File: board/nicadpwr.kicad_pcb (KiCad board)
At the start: 2 copper layers, 60.2 x 20.6 mm, 31 parts, among them P1 CONN_SENSE, P2 CONN_CHARGE, P3 CONN_BAT, P4 CONN_VOUT, Q1 2N7000, Q2 BC547, Q3 TPCA8052H, U1 LM317T, U2 LM1117-5.0, U3 MC34063A

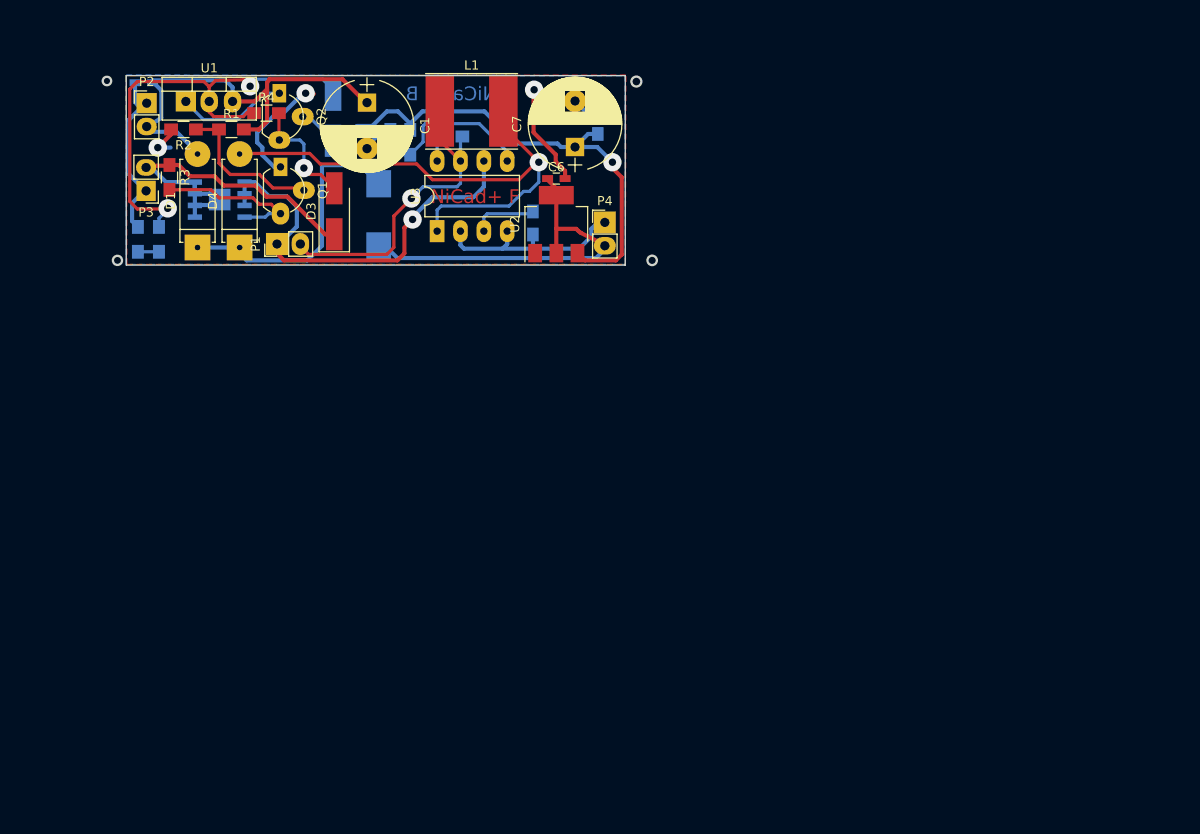
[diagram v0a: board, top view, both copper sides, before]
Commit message: Redesign of the board with fixes...
1. The charging voltage is now 5V (suitable for charging from USB)
   The charging now is connected directly to boost converter and
   linear out and battery charger are connected to the boost output.
   The converter raises battery or charging voltage to 6.3 volt.
2. Fixed problem with n-channel FET switch by using p-channel high
   side FET.
3. The board is enlarged and made single copper layer.
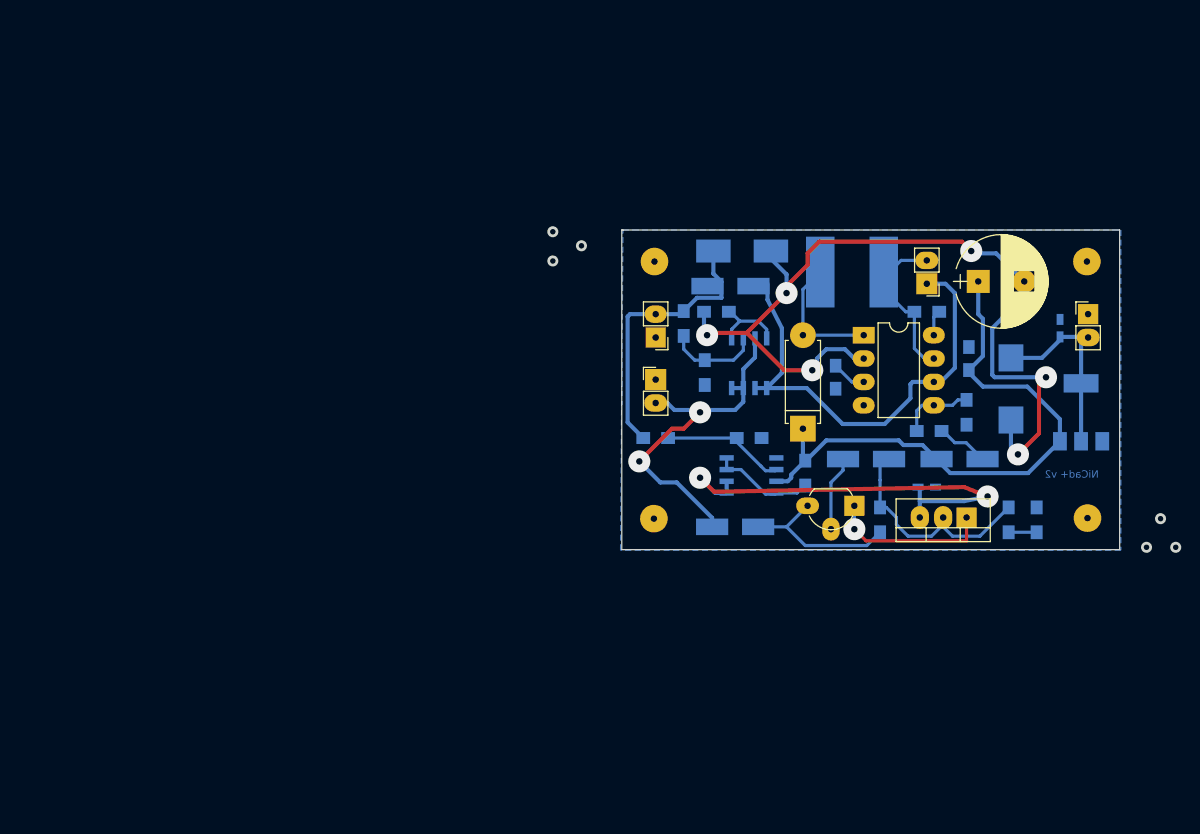
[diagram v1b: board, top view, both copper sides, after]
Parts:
- added D6: RS1M, Diodes_SMD:D_SMA_Handsoldering, B.Cu at (133.1, 79.5)
- added R10: 100K, Resistors_SMD:R_0805_HandSoldering, B.Cu at (110.2, 77.2)
- added R11: 100K, Resistors_SMD:R_0805_HandSoldering, B.Cu at (116.3, 81.0)
- added R9: 100, Resistors_SMD:R_0805_HandSoldering, B.Cu at (100.1, 77.2)
- added REF**: MountingHole_3mm, Mounting_Holes:MountingHole_3mm, F.Cu at (146.9, 58.0)
- added REF**: MountingHole_3mm, Mounting_Holes:MountingHole_3mm, F.Cu at (99.9, 58.0)
- added REF**: MountingHole_3mm, Mounting_Holes:MountingHole_3mm, F.Cu at (99.9, 86.0)
- added REF**: MountingHole_3mm, Mounting_Holes:MountingHole_3mm, F.Cu at (147.0, 85.9)
- C1: value 470uF -> 100uF; footprint Capacitors_ThroughHole:CP_Radial_D10.0mm_P5.00mm -> Capacitors_Tantalum_SMD:CP_Tantalum_Case-U_EIA-6032-15_Hand; moved to B.Cu
- C6, L1, R4, U2: moved to B.Cu
- D1: value 1N3600 -> RS1M; footprint Diodes_ThroughHole:D_5W_P10.16mm_Horizontal -> Diodes_SMD:D_SMA_Handsoldering; moved to B.Cu
- D2: value 1N4148 -> RS1M
- D3: value 1N4148 -> RS1M; moved to B.Cu
- D4: value 1N3600 -> 1N5819
- Q1: value 2N7000 -> Si4562DY; footprint nicadpwr:2N7000-TO92 -> Housings_SOIC:SOIC-8_3.9x4.9mm_Pitch1.27mm; moved to B.Cu
- Q3: value TPCA8052H -> Si4562DY; footprint nicadpwr:TPCA8052H -> Housings_SOIC:SOIC-8_3.9x4.9mm_Pitch1.27mm
- R1: value 100K -> 100; moved to B.Cu
- R2, R3: value 330K -> 100K; moved to B.Cu
- R5: value 9.2K -> 100K
- R6: value 2.2K -> 27K
- moved D5 102.3 mm to (141.5, 86.1)
- moved R8 97.2 mm to (138.4, 86.1)
- moved U1 96.1 mm to (133.9, 85.9), turned to 180 degrees
- moved C2 95.8 mm to (129.5, 82.5), turned to 0 degrees
- moved R4 80.0 mm to (124.5, 86.1), turned to 270 degrees
- moved Q2 76.9 mm to (121.7, 84.6), turned to 180 degrees
- moved C5 71.3 mm to (138.7, 71.9), turned to 270 degrees
- moved P1 70.7 mm to (129.5, 60.5), turned to 180 degrees
- moved R6 69.1 mm to (133.9, 74.4), turned to 270 degrees
- moved D2 68.8 mm to (122.9, 79.5), turned to 0 degrees
- moved Q3 65.1 mm to (110.5, 81.3)
- moved R5 64.5 mm to (129.8, 76.5), turned to 180 degrees
- moved D4 64.3 mm to (116.1, 76.2)
- moved R2 62.5 mm to (105.4, 70.1), turned to 270 degrees
- moved R3 61.2 mm to (106.7, 63.5), turned to 180 degrees
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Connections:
- C2 pad 1: /VCHARGE -> /CHARGE_IN
- D1 pad 1: /BOOST_OUT -> /BOOST_IN
- Q1 pad 3: Earth -> /VBAT
- Q3 pad 1: /VBAT -> Earth
- Q3 pad 2: Net-(Q1-Pad1) -> Net-(Q3-Pad2)
- Q3 pad 3: /BOOST_IN -> /BOOST_OUT
- R3 pad 1: /VBAT -> Net-(Q1-Pad1)
- R3 pad 2: Net-(Q1-Pad1) -> Earth
- R5 pad 1: Net-(R5-Pad1) -> Net-(D6-Pad1)
- R5 pad 2: /BOOST_OUT -> Net-(R5-Pad2)
- R6 pad 1: Net-(R5-Pad1) -> Net-(R5-Pad2)
- U1 pad 3: /VCHARGE -> /CHARGE_IN
- U3 pad 5: Net-(R5-Pad1) -> Net-(R5-Pad2)
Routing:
- net /CHARGE_IN: track 0.00 -> 47.7 mm, vias 0 -> 2
- net Net-(D4-Pad2): track 57.8 -> 14.2 mm, vias 1 -> 0
- net Net-(D2-Pad2): track 51.7 -> 25.0 mm, vias 2 -> 0
- net /VOUT: track 40.5 -> 21.1 mm
- net /BOOST_OUT: track 83.3 -> 64.5 mm, vias 1 -> 0
- net /VCHARGE: track 48.1 -> 30.4 mm
- net Net-(R5-Pad1): track 17.3 -> 0.00 mm
- net Net-(L1-Pad1): track 33.9 -> 18.0 mm, vias 1 -> 0
- net Net-(Q3-Pad2): track 0.00 -> 13.5 mm
- net Earth: track 85.3 -> 97.1 mm, vias 3 -> 6
- net Net-(Q3-Pad4): track 0.00 -> 11.3 mm
- net Net-(Q1-Pad1): track 17.2 -> 8.12 mm
- net Net-(R5-Pad2): track 0.00 -> 8.11 mm
- net Net-(Q1-Pad2): track 16.5 -> 10.2 mm
- net Net-(D6-Pad1): track 0.00 -> 5.71 mm
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- removed copper zone on F.Cu, net Earth
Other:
- board size 60.2 x 20.6 mm -> 68.6 x 35.2 mm
- net class Default: via_dia 2 -> 2.4; via_drill 0.8 -> 0.7
- net class PWR: via_dia 2 -> 2.4; via_drill 0.8 -> 0.7
- net class RF removed
- rule pad_to_mask_clearance: 0.2 -> 0
- rule trace_min: 0.1 -> 0.2
- board text added: "NiCad+ v2"
- board text removed: "NiCad+ B"
- board text removed: "NiCad+ F"

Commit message: Rdesign of the board for v3
The new version moves boost converter and charger out
of the main path to be active only when charging.
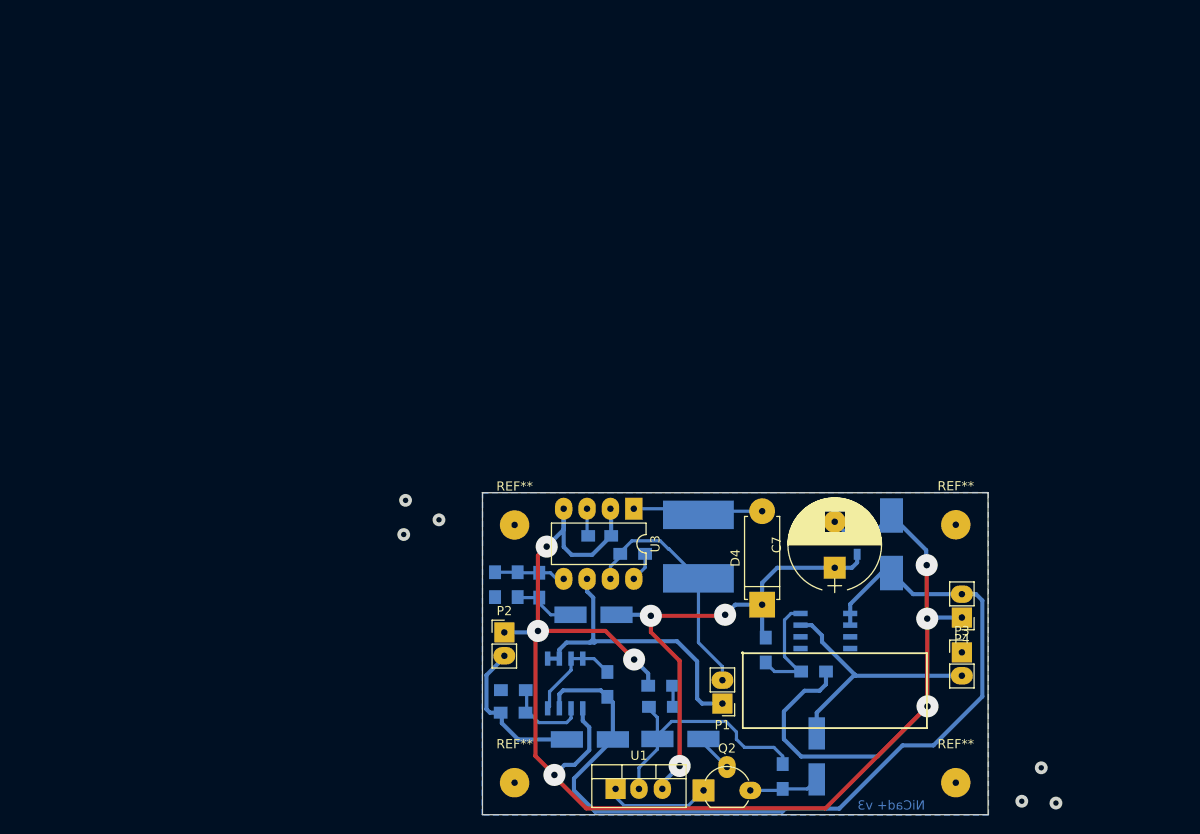
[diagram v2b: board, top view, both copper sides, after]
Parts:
- removed C3: 10uF, Capacitors_SMD:C_0805_HandSoldering
- removed C5: 22uF, Capacitors_Tantalum_SMD:CP_Tantalum_Case-X_EIA-7343-43_Wave
- removed C6: 100nF, Capacitors_SMD:C_0603_HandSoldering
- removed the REF** at (146.9, 58.0)
- removed the REF** at (99.9, 58.0)
- removed the REF** at (99.9, 86.0)
- removed the REF** at (147.0, 85.9)
- removed U2: LM1117-5.0, TO_SOT_Packages_SMD:SOT-223
- added REF**: MountingHole_3.2mm_M3, Mounting_Holes:MountingHole_3.2mm_M3, F.Cu at (84.7, 86.7)
- added REF**: MountingHole_3.2mm_M3, Mounting_Holes:MountingHole_3.2mm_M3, F.Cu at (132.7, 86.6)
- added REF**: MountingHole_3.2mm_M3, Mounting_Holes:MountingHole_3.2mm_M3, F.Cu at (132.7, 114.7)
- added REF**: MountingHole_3.2mm_M3, Mounting_Holes:MountingHole_3.2mm_M3, F.Cu at (84.7, 114.7)
- C4: value 1nF -> 700pF
- C7: value 470uF -> 1000uF
- R1: value 100 -> 330K
- R10, R3: value 100K -> 47K
- R2: value 100K -> 100
- R5: value 100K -> 330K
- moved R6 54.6 mm to (82.6, 93.2)
- moved D1 51.6 mm to (92.9, 110.0)
- moved P1 50.7 mm to (107.3, 106.1)
- moved U1 48.2 mm to (95.7, 115.3), turned to 0 degrees
- moved R5 45.6 mm to (87.4, 93.2), turned to 90 degrees
- moved D5 44.7 mm to (100.6, 104.1), turned to 0 degrees
- moved P3 44.6 mm to (133.3, 100.5)
- moved D6 43.2 mm to (93.3, 96.4), turned to 0 degrees
- moved R8 42.9 mm to (100.7, 106.4), turned to 0 degrees
- moved R7 41.4 mm to (97.6, 89.8)
- moved R3 40.5 mm to (117.2, 102.6), turned to 0 degrees
- moved R10 37.5 mm to (84.6, 104.6), turned to 180 degrees
- moved D2 36.5 mm to (102.8, 109.9), turned to 180 degrees
- moved P2 36.0 mm to (83.6, 98.3), turned to 0 degrees
- moved C1 35.8 mm to (125.7, 88.8), turned to 90 degrees
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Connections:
- C1 pad 1: /VCHARGE -> /VOUT
- C2 pad 1: /CHARGE_IN -> /BOOST_OUT
- D1 pad 1: /BOOST_IN -> /VOUT
- Q1 pad 1: Net-(Q1-Pad1) -> (no net)
- Q1 pad 2: Net-(Q1-Pad2) -> (no net)
- Q1 pad 4: Net-(Q1-Pad1) -> Net-(Q1-Pad4)
- Q1 pad 5: /BOOST_IN -> /VOUT
- Q1 pad 6: /BOOST_IN -> /VOUT
- Q1 pad 7: /VBAT -> (no net)
- Q1 pad 8: /VBAT -> (no net)
- Q3 pad 3: /BOOST_OUT -> /VOUT
- Q3 pad 5: /CHARGE_IN -> /BOOST_IN
- Q3 pad 6: /CHARGE_IN -> /BOOST_IN
- R1 pad 1: Net-(Q1-Pad2) -> Net-(D6-Pad1)
- R1 pad 2: /VCHARGE -> Net-(R1-Pad2)
- R11 pad 1: /BOOST_OUT -> /VOUT
- R2 pad 1: Net-(Q1-Pad2) -> Net-(Q1-Pad4)
- R2 pad 2: Earth -> /BOOST_OUT
- R3 pad 1: Net-(Q1-Pad1) -> Net-(Q1-Pad4)
- R5 pad 2: Net-(R5-Pad2) -> Net-(R1-Pad2)
- R6 pad 1: Net-(R5-Pad2) -> Net-(R1-Pad2)
- U1 pad 3: /CHARGE_IN -> /BOOST_OUT
- U3 pad 5: Net-(R5-Pad2) -> Net-(R1-Pad2)
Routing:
- net Earth: track 97.1 -> 182.8 mm, vias 6 -> 7
- net /VOUT: track 21.1 -> 99.6 mm
- net /CHARGE_IN: track 47.7 -> 0.00 mm, vias 2 -> 0
- net /BOOST_IN: track 50.7 -> 33.9 mm
- net /VCHARGE: track 30.4 -> 17.3 mm
- net Net-(Q1-Pad4): track 0.00 -> 12.8 mm
- net Net-(L1-Pad1): track 18.0 -> 29.6 mm
- net /VBAT: track 39.5 -> 28.3 mm, vias 2 -> 0
- net Net-(D3-Pad2): track 17.9 -> 7.71 mm
- net Net-(Q1-Pad2): track 10.2 -> 0.00 mm
- net /BOOST_OUT: track 64.5 -> 56.2 mm, vias 0 -> 3
- net Net-(Q1-Pad1): track 8.12 -> 0.00 mm
- net Net-(R5-Pad2): track 8.11 -> 0.00 mm
- net Net-(R1-Pad2): track 0.00 -> 7.82 mm
- net Net-(Q2-Pad1): track 17.8 -> 11.5 mm, vias 1 -> 0
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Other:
- board size 68.6 x 35.2 mm -> 71.9 x 35 mm
- board text added: "NiCad+ v3"
- board text removed: "NiCad+ v2"

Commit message: Fix bugs to finaly get working board ...
1. Upper rail for the sense opamp was set to +4V which holds its
output under 1V. This is not enough for control of the MSP which
is expected to be around 1.25V. Changed the upper rail to BOOST_OUT.

2. Signal controlling Q1 battery switch was connected to BOOST_OUT.
This works, but when charger is disconnected boost out capaccitor
discharges relatively slowly and opens Q1 with considerable delay.
Changed the Q1 control to VCHARGE instead.
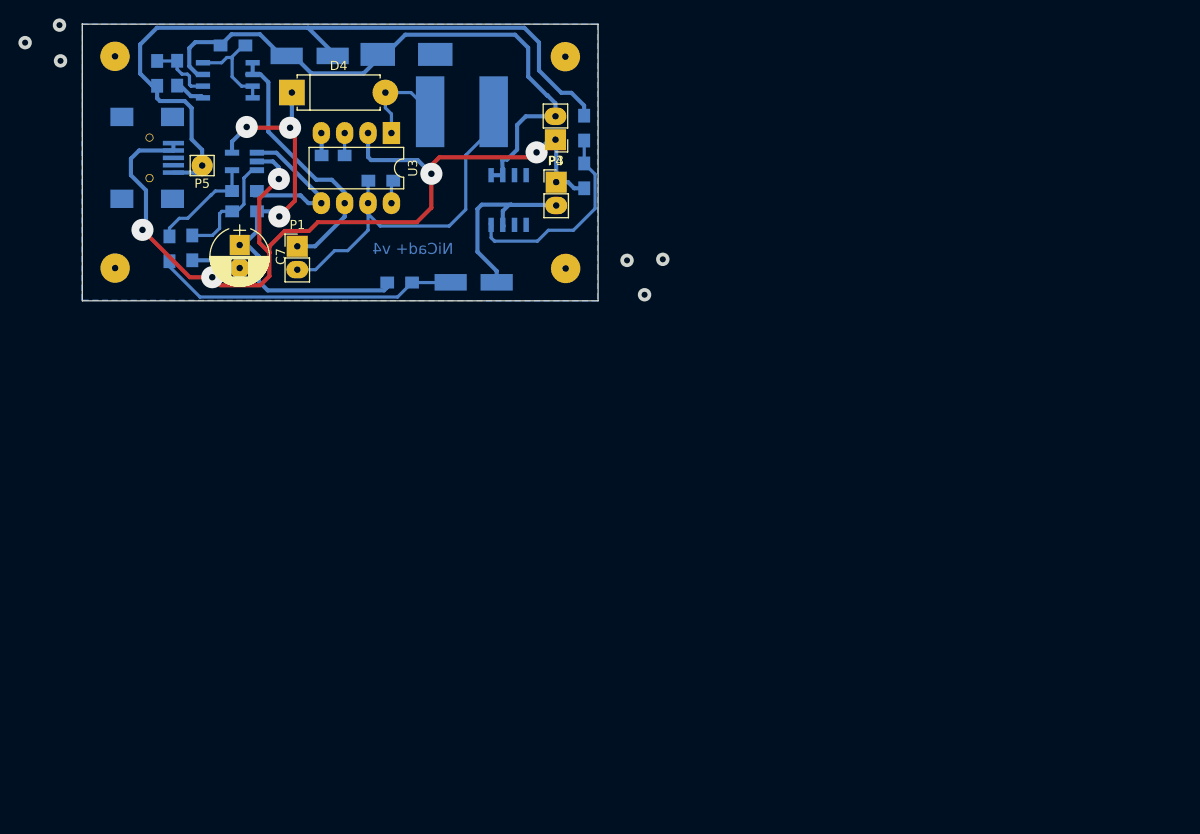
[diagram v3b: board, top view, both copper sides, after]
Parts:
- removed C2: 100nF, Capacitors_SMD:C_0603_HandSoldering
- removed D3, D6: RS1M, Diodes_SMD:D_SMA_Handsoldering
- removed D5: LED, LEDs:LED_0805_HandSoldering
- removed Q2: BC547, TO_SOT_Packages_THT:TO-92_Molded_Wide_Oval
- removed the REF** at (84.7, 86.7)
- removed the REF** at (132.7, 86.6)
- removed the REF** at (132.7, 114.7)
- removed the REF** at (84.7, 114.7)
- added P5: TP1_VCHARGE, Connect:Pin_d0.9mm_L10.0mm_W2.4mm_FlatFork, F.Cu at (50.8, 47.6)
- added REF**: MountingHole_3.2mm_M3, Mounting_Holes:MountingHole_3.2mm_M3, F.Cu at (41.3, 35.7)
- added REF**: MountingHole_3.2mm_M3, Mounting_Holes:MountingHole_3.2mm_M3, F.Cu at (41.3, 58.8)
- added REF**: MountingHole_3.2mm_M3, Mounting_Holes:MountingHole_3.2mm_M3, F.Cu at (90.3, 58.8)
- added REF**: MountingHole_3.2mm_M3, Mounting_Holes:MountingHole_3.2mm_M3, F.Cu at (90.3, 35.8)
- C7: value 1000uF -> 220uF; footprint Capacitors_ThroughHole:CP_Radial_D10.0mm_P5.00mm -> Capacitors_ThroughHole:CP_Radial_D6.3mm_P2.50mm
- P2: value CONN_CHARGE -> USB_B; footprint Socket_Strips:Socket_Strip_Straight_1x02_Pitch2.54mm -> Connect:USB_Mini-B; moved to B.Cu
- R1, R5: value 330K -> 100K
- R4: value 22 -> 100K
- R6: value 27K -> 100K
- R8: value 200 -> 22
- U1: value LM317T -> OPA237NA; footprint nicadpwr:LM317T-TO220 -> TO_SOT_Packages_SMD:SOT-23-5_HandSoldering; moved to B.Cu
- moved R4 86.1 mm to (49.7, 56.6)
- moved R11 80.5 mm to (54.1, 34.6), turned to 0 degrees
- moved D1 80.3 mm to (62.5, 35.7), turned to 0 degrees
- moved R9 79.5 mm to (45.9, 37.6), turned to 270 degrees
- moved U1 79.2 mm to (55.4, 47.2), turned to 180 degrees
- moved R10 76.3 mm to (48.1, 37.6), turned to 270 degrees
- moved D4 75.6 mm to (60.5, 39.7), turned to 0 degrees
- moved Q3 75.1 mm to (53.6, 38.3), turned to 0 degrees
- moved C1 74.9 mm to (73.0, 35.5), turned to 0 degrees
- moved C7 73.6 mm to (54.9, 56.2), turned to 270 degrees
- moved P4 68.2 mm to (89.2, 44.8)
- moved P1 67.8 mm to (61.1, 56.4), turned to 0 degrees
- moved P3 67.5 mm to (89.3, 49.4)
- moved P2 64.5 mm to (44.9, 46.8)
- moved R2 60.0 mm to (92.3, 43.5)
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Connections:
- D2 pad 1: Net-(D2-Pad1) -> /VBAT
- P2 pad 1: Earth -> /VCHARGE
- P2 pad 2: /VCHARGE -> (no net)
- R1 pad 1: Net-(D6-Pad1) -> Net-(R1-Pad1)
- R1 pad 2: Net-(R1-Pad2) -> /BOOST_CTRL
- R2 pad 2: /BOOST_OUT -> /VCHARGE
- R4 pad 1: Net-(D2-Pad2) -> Net-(R4-Pad1)
- R4 pad 2: Net-(D3-Pad2) -> Earth
- R5 pad 1: Net-(D6-Pad1) -> Net-(R4-Pad1)
- R5 pad 2: Net-(R1-Pad2) -> /BOOST_OUT
- R6 pad 1: Net-(R1-Pad2) -> Net-(R1-Pad1)
- R6 pad 2: Earth -> Net-(D2-Pad2)
- R8 pad 1: Net-(D2-Pad2) -> /BOOST_OUT
- R8 pad 2: Net-(D5-Pad2) -> Net-(D2-Pad2)
- U1 pad 1: Net-(Q2-Pad1) -> /BOOST_CTRL
- U1 pad 2: Net-(D2-Pad2) -> Earth
- U1 pad 3: /BOOST_OUT -> Net-(R4-Pad1)
- U3 pad 5: Net-(R1-Pad2) -> /BOOST_CTRL
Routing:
- net Earth: track 182.8 -> 119.1 mm, vias 7 -> 5
- net /VCHARGE: track 17.3 -> 80.9 mm
- net /VOUT: track 99.6 -> 67.7 mm
- net /BOOST_CTRL: track 0.00 -> 17.3 mm
- net Net-(R4-Pad1): track 0.00 -> 12.6 mm
- net Net-(R1-Pad1): track 0.00 -> 11.7 mm
- net Net-(Q2-Pad1): track 11.5 -> 0.00 mm
- net Net-(L1-Pad1): track 29.6 -> 40.4 mm
- net Net-(Q1-Pad4): track 12.8 -> 22.5 mm
- net Net-(R1-Pad2): track 7.82 -> 0.00 mm
- net /VBAT: track 28.3 -> 20.5 mm
- net Net-(D3-Pad2): track 7.71 -> 0.00 mm
- net Net-(D6-Pad1): track 6.89 -> 0.00 mm
- net Net-(D2-Pad2): track 27.9 -> 33.7 mm
- net /BOOST_OUT: track 56.2 -> 50.5 mm
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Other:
- board size 71.9 x 35 mm -> 70.4 x 30.5 mm
- board text added: "NiCad+ v4"
- board text removed: "NiCad+ v3"
